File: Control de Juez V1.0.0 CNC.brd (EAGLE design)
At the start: 35.5 x 58.4 mm, 31 parts, among them IC1 MEGA48/88/168-AU, Q1 MMBT3904, Q2 MMBT3904, Q3 MMBT3904, SW1 JS202011CQN, SW2 3-1825910-1, SW3 3-1825910-1, SW4 3-1825910-1

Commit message: Add files via upload
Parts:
- removed C2, C3: 0.1uF, rcl:C0603
- removed IC1: MEGA48/88/168-AU, avr-8:TQFP32-08
- removed JP2: (no value), pinhead-2:1X04-S
- removed L1: 10uH, rcl:L1812
- removed R1, R7, R8, R9: 10K, rcl:R0603
- removed SW1: JS202011CQN, C&K-Slider_Switch:PTH
- added PROG: (no value), pinhead:1X03
- added S1: JS102011SAQN, JS102011SAQN:SW_JS102011SAQN
- added U1: ATTINY412-SSNSOIC8_SA_SST_MCH-M, attiny412:SOIC8_SA_SST_MCH-M
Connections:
- removed net N$2: C3.1, IC1.18, L1.1
- removed net N$3: C2.1, IC1.20
- removed net N$4: IC1.16, JP2.1
- removed net N$5: IC1.17, JP2.2
- removed net N$6: JP3.1, SW1.1.1, SW1.1.2, SW1.2.1, SW1.2.2
- removed net RESET: IC1.29, JP2.3, R1.1
- new net BAT+: JP3.1, S1.2, S1.3
- net +5V: now also PROG.1, S1.1, U1.1; no longer IC1.4, IC1.6, L1.2, R1.2, R7.2, R8.2, R9.2, SW1.3.1, SW1.3.2
- net GND: now also PROG.3, U1.8; no longer C2.2, C3.2, IC1.21, IC1.3, IC1.5
- net GO: now also U1.3; no longer IC1.31, R9.1
- net LEDS: now also U1.5; no longer IC1.13
- net LEDSMD: now also U1.4; no longer IC1.32
- net N$1: now also PROG.2, U1.6; no longer IC1.15, JP2.4
- net READY: now also U1.2; no longer IC1.1, R7.1
- net RST: now also U1.7; no longer IC1.30, R8.1
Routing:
- net +5V: track 203.4 -> 62.7 mm, vias 4 -> 1
- net GND: track 130.3 -> 58.4 mm, vias 5 -> 3
- net LEDS: track 91.3 -> 42.3 mm
- net GO: track 48.5 -> 6.50 mm, vias 1 -> 0
- net RESET: track 29.4 -> 0.00 mm, vias 2 -> 0
- net READY: track 34.2 -> 6.51 mm, vias 1 -> 0
- net RST: track 33.0 -> 6.51 mm, vias 2 -> 0
- net N$2: track 17.3 -> 0.00 mm
- net LEDSMD: track 46.1 -> 29.0 mm
- net N$6: track 13.3 -> 0.00 mm
- net N$1: track 13.1 -> 0.00 mm, vias 1 -> 0
- net N$5: track 10.4 -> 0.00 mm, vias 1 -> 0
- net N$3: track 10.1 -> 0.00 mm
- net N$4: track 8.63 -> 0.00 mm, vias 1 -> 0

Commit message: Add files via upload
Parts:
- removed JP1, JP3: (no value), pinhead-2:1X02-S
- removed LED4: (no value), led:CHIP-LED0603
- removed PROG: (no value), pinhead:1X03
- removed Q2, Q3: MMBT3904, FAIRCHILD-MMBT3904_Transistor:SOT23
- removed R3, R4: 1K, rcl:R0603
- removed R5: 330E, rcl:R0603
- removed SW2, SW3, SW4: 3-1825910-1, TE-Push_button:TE_3-1825910-1
- added BT2: BU2032SM-HD-G, BU2032SM-HD-G:BAT_BU2032SM-HD-G
- added GND, UPDI, V+: TPB1,27, testpad:B1,27
- added GO, READY, RESET: EVQ-P7L01P, EVQ-P7L01P:SW_EVQ-P7L01P
- added GOLD_ORB_SM1: OSHWLOGOLOGO8MM, oshw:OSHW_8MM
- added R1: 1K, rcl:R0603
- BT1: value HOLD-BATTERY-3-AAA -> BU2032SM-HD-G; device BATTERY_HOLDER_3AAA-C9091:HOLDER-3-AAA -> BU2032SM-HD-G:BAT_BU2032SM-HD-G
- LED5: device led:CHIP-LED0603 -> led:SML1206
- R6: value 330E -> 1k
- moved U1 55.7 mm to (17.9, 48.9), flipped to the bottom
- moved S1 53.9 mm to (2.54, 53.3), flipped to the bottom
- moved C4 49.9 mm to (17.8, 55.2), flipped to the bottom, turned to 0 degrees
- moved C1 46.6 mm to (17.8, 52.7), flipped to the bottom, turned to 0 degrees
- moved Q1 21.6 mm to (11.4, 61.0), flipped to the bottom, turned to 270 degrees
- moved R2 21.6 mm to (15.2, 61.0), flipped to the bottom, turned to 270 degrees
- moved LED5 16.3 mm to (25.9, 58.2), flipped to the bottom
- moved R6 15.3 mm to (19.9, 58.4), flipped to the bottom, turned to 180 degrees
- moved BT1 15.2 mm to (17.8, 11.5), flipped to the bottom
- moved LED1 8.89 mm to (31.8, 64.8)
- moved LED2 8.89 mm to (17.8, 64.8), flipped to the bottom
- moved LED3 8.89 mm to (3.81, 64.8)
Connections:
- removed net BAT+: JP3.1, S1.2, S1.3
- removed net N$10: Q3.B, R4.1
- removed net N$11: Q2.B, R3.1
- removed net N$13: LED5.C, R5.1
- removed net N$15: LED4.A, R5.2
- removed net N$7: LED1.2, Q1.C
- removed net N$8: LED2.2, Q2.C
- removed net N$9: LED3.2, Q3.C
- new net N$2: BT1.-, BT2.-, S1.1, S1.2
- new net N$3: LED1.2, LED2.2, LED3.2, R1.1
- new net N$4: Q1.C, R1.2
- net +5V: now also BT1.+, BT2.+, V+.TP; no longer JP1.1, PROG.1, S1.1
- net GND: now also GND.TP, GO.1_1, GO.1_2, READY.1_1, READY.1_2, RESET.1_1, RESET.1_2, S1.3; no longer JP1.2, JP3.2, PROG.3, Q2.E, Q3.E, SW2.1, SW2.2, SW3.1, SW3.2, SW4.1, SW4.2
- net GO: now also GO.2_1, GO.2_2; no longer SW4.3, SW4.4
- net LEDS: no longer R3.2, R4.2
- net LEDSMD: now also LED5.C; no longer LED4.C
- net N$1: now also UPDI.TP; no longer PROG.2
- net READY: now also READY.2_1, READY.2_2; no longer SW2.3, SW2.4
- net RST: now also RESET.2_1, RESET.2_2; no longer SW3.3, SW3.4
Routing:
- net +5V: track 62.7 -> 129.4 mm, vias 1 -> 2
- net N$2: track 0.00 -> 42.9 mm
- net N$3: track 0.00 -> 33.3 mm
- net READY: track 6.51 -> 25.6 mm, vias 0 -> 2
- net GND: track 58.4 -> 77.2 mm, vias 3 -> 4
- net N$13: track 18.4 -> 0.00 mm, vias 2 -> 0
- net LEDS: track 42.3 -> 24.3 mm
- net RST: track 6.51 -> 22.5 mm, vias 0 -> 2
- net N$8: track 12.8 -> 0.00 mm, vias 1 -> 0
- net LEDSMD: track 29.0 -> 17.0 mm
- net GO: track 6.50 -> 17.9 mm, vias 0 -> 2
- net N$9: track 7.59 -> 0.00 mm, vias 1 -> 0
- net N$7: track 4.80 -> 0.00 mm, vias 1 -> 0
- net N$10: track 4.03 -> 0.00 mm
- net N$11: track 4.03 -> 0.00 mm
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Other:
- board size 35.5 x 58.4 mm -> 35.5 x 67.3 mm
- board text added: "Apagado"
- board text added: "Control Juez Anti Fuckin' Monopolio CNC V1.1.0"
- board text added: "Diseñado en México por Sol y Nomada-e"
- board text added: "Encendido"
- board text added: "GO"
- board text added: "READY"
- board text added: "RESET"
- board text removed: "Control Juez Anti Fuckin' Monopolio CNC V1.0.0"

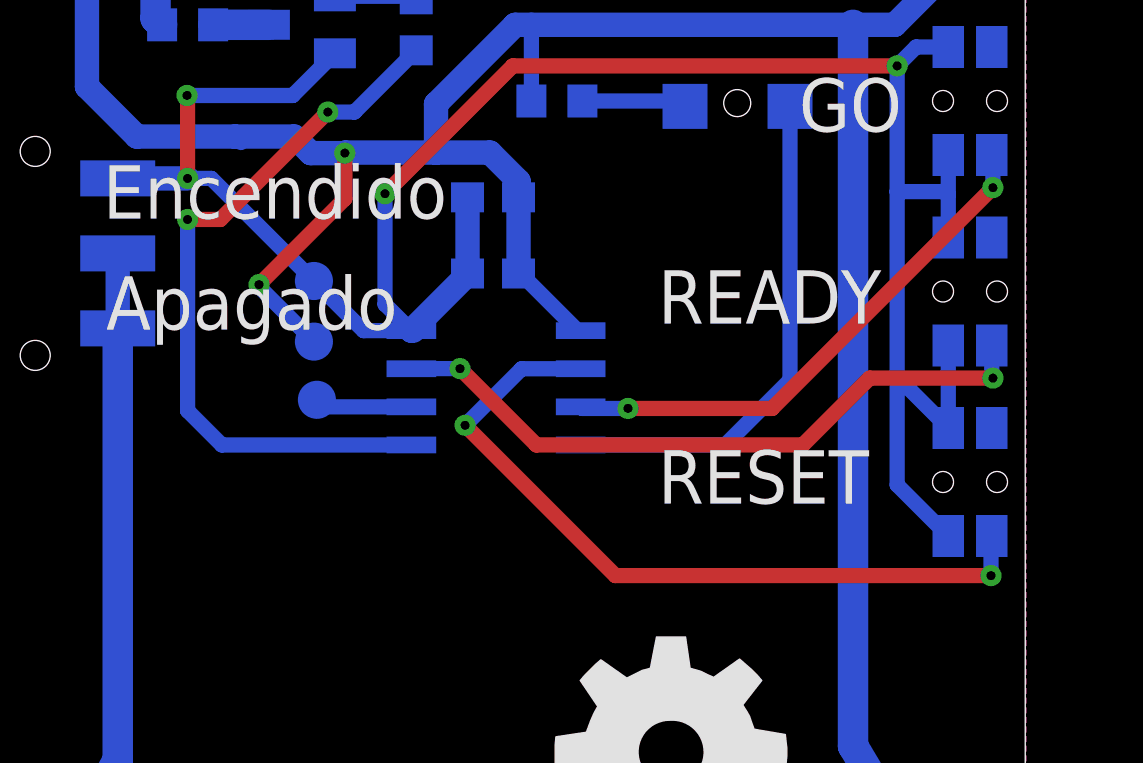
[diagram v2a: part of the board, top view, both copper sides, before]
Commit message: Add files via upload
Reconexiones para mejor programación ocupando el hardware del microcontrolador
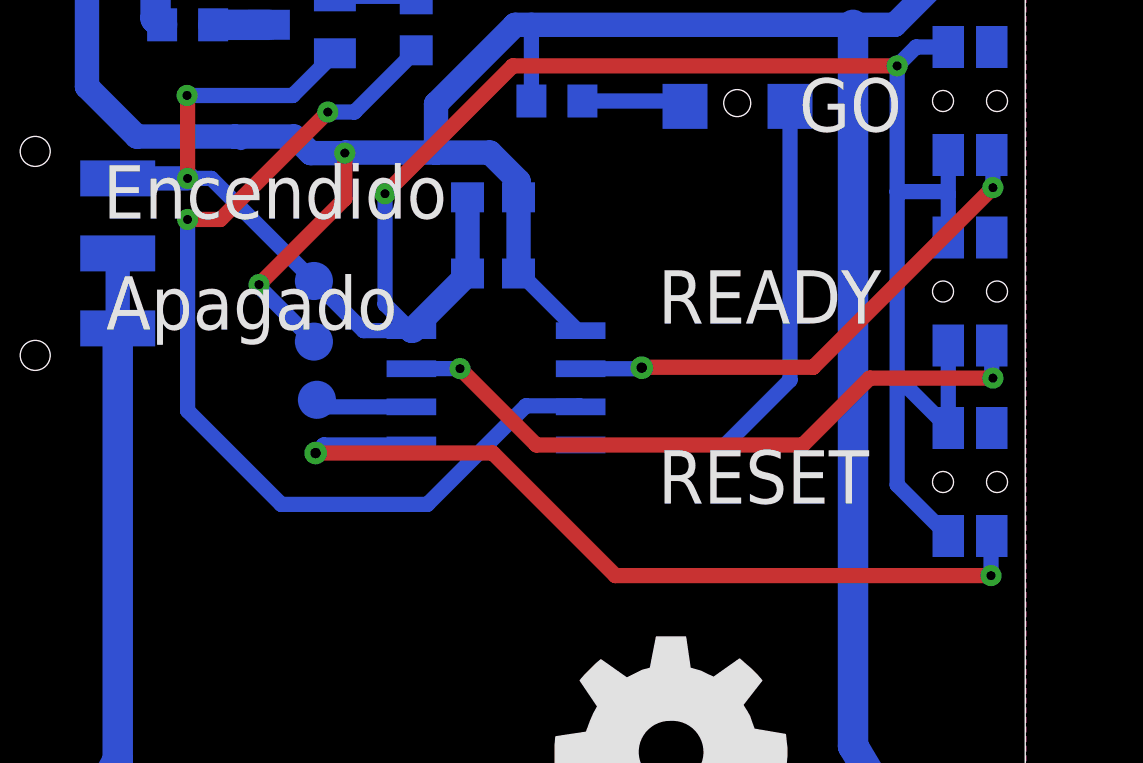
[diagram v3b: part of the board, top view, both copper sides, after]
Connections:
- net GO: now also U1.2; no longer U1.3
- net LEDS: now also U1.3; no longer U1.5
- net READY: now also U1.5; no longer U1.2
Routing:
- net LEDS: track 24.3 -> 32.1 mm
- net LEDSMD: track 17.0 -> 12.2 mm
- net READY: track 25.6 -> 28.8 mm
- net GO: track 17.9 -> 17.3 mm
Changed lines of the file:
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@@
 <signal name="LEDS">
 <contactref element="R2" pad="2"/>
-<contactref element="U1" pad="5"/>
 <wire x1="15.24" y1="60.11" x2="13.181775" y2="58.051775" width="0.508" layer="16"/>
 <wire x1="13.181775" y1="58.051775" x2="12.29259375" y2="58.051775" width="0.508" layer="16"/>
@@
 <wire x1="8.71161875" y1="54.4708" x2="7.62" y2="54.4708" width="0.508" layer="1"/>
 <via x="7.62" y="54.4708" extent="1-16" drill="0.3"/>
-<wire x1="7.62" y1="48.0947" x2="8.7597" y2="46.955" width="0.508" layer="16"/>
-<wire x1="8.7597" y1="46.955" x2="15.07865" y2="46.955" width="0.508" layer="16"/>
 <wire x1="7.62" y1="54.4708" x2="7.62" y2="48.0947" width="0.508" layer="16"/>
+<contactref element="U1" pad="3"/>
+<wire x1="10.7405" y1="44.9742" x2="15.6118" y2="44.9742" width="0.508" layer="16"/>
+<wire x1="15.6118" y1="44.9742" x2="18.8976" y2="48.26" width="0.508" layer="16"/>
+<wire x1="18.8976" y1="48.26" x2="20.68635" y2="48.26" width="0.508" layer="16"/>
+<wire x1="20.68635" y1="48.26" x2="20.72135" y2="48.225" width="0.508" layer="16"/>
+<wire x1="7.62" y1="48.0947" x2="10.7405" y2="44.9742" width="0.508" layer="16"/>
 </signal>
 <signal name="N$14">
@@
 </signal>
 <signal name="LEDSMD">
-<contactref element="U1" pad="4"/>
 <contactref element="LED5" pad="C"/>
-<wire x1="20.72135" y1="46.955" x2="25.54" y2="46.955" width="0.508" layer="16"/>
 <wire x1="25.54" y1="46.955" x2="27.7" y2="49.115" width="0.508" layer="16"/>
 <wire x1="27.7" y1="49.115" x2="27.7" y2="58.24" width="0.508" layer="16"/>
+<contactref element="U1" pad="4"/>
+<wire x1="20.72135" y1="46.955" x2="25.54" y2="46.955" width="0" layer="19" extent="16-16"/>
 </signal>
 <signal name="RST">
@@
 <wire x1="30.3545125" y1="49.1828" x2="28.1267125" y2="46.955" width="0.508" layer="1"/>
 <wire x1="28.1267125" y1="46.955" x2="19.245" y2="46.955" width="0.508" layer="1"/>
-<wire x1="19.245" y1="46.955" x2="16.7" y2="49.5" width="0.508" layer="1"/>
 <wire x1="16.7" y1="49.5" x2="15.08365" y2="49.5" width="0.508" layer="16"/>
 <wire x1="15.08365" y1="49.5" x2="15.07865" y2="49.495" width="0.508" layer="16"/>
+<wire x1="19.245" y1="46.955" x2="16.7" y2="49.5" width="0.508" layer="1"/>
 <wire x1="34.425" y1="50.27" x2="34.425" y2="53.87" width="0" layer="19" extent="16-16"/>
 </signal>
 <signal name="GO">
-<contactref element="U1" pad="3"/>
 <contactref element="GO" pad="2_2"/>
 <contactref element="GO" pad="2_1"/>
@@
 <wire x1="34.4628" y1="56.5822" x2="34.4628" y2="55.5328" width="0.508" layer="16"/>
 <via x="34.4628" y="55.5328" extent="1-16" drill="0.3"/>
-<wire x1="34.4628" y1="55.5328" x2="27.1018" y2="48.1718" width="0.508" layer="1"/>
-<wire x1="27.1018" y1="48.1718" x2="22.3" y2="48.1718" width="0.508" layer="1"/>
-<via x="22.3" y="48.1718" extent="1-16" drill="0.3"/>
-<wire x1="22.3" y1="48.1718" x2="20.77455" y2="48.1718" width="0.508" layer="16"/>
-<wire x1="20.77455" y1="48.1718" x2="20.72135" y2="48.225" width="0.508" layer="16"/>
+<wire x1="34.4628" y1="55.5328" x2="28.4734" y2="49.5434" width="0.508" layer="1"/>
+<contactref element="U1" pad="2"/>
+<wire x1="28.4734" y1="49.5434" x2="22.7718" y2="49.5434" width="0.508" layer="1"/>
+<wire x1="22.7584" y1="49.53" x2="22.7718" y2="49.5434" width="0.508" layer="1"/>
+<via x="22.7584" y="49.53" extent="1-16" drill="0.35"/>
+<wire x1="22.7584" y1="49.53" x2="22.7234" y2="49.495" width="0.508" layer="16"/>
+<wire x1="22.7234" y1="49.495" x2="20.72135" y2="49.495" width="0.508" layer="16"/>
 <wire x1="34.425" y1="56.62" x2="34.425" y2="60.22" width="0" layer="19" extent="16-16"/>
 </signal>
 <signal name="READY">
-<contactref element="U1" pad="2"/>
 <contactref element="READY" pad="2_2"/>
 <contactref element="READY" pad="2_1"/>
@@
 <via x="34.4" y="42.6" extent="1-16" drill="0.3"/>
 <wire x1="34.4" y1="42.6" x2="21.87918125" y2="42.6" width="0.508" layer="1"/>
-<wire x1="21.87918125" y1="42.6" x2="16.8689" y2="47.61028125" width="0.508" layer="1"/>
-<via x="16.8689" y="47.61028125" extent="1-16" drill="0.3"/>
-<wire x1="16.8689" y1="47.61028125" x2="18.75361875" y2="49.495" width="0.508" layer="16"/>
-<wire x1="18.75361875" y1="49.495" x2="20.72135" y2="49.495" width="0.508" layer="16"/>
+<contactref element="U1" pad="5"/>
+<wire x1="21.87918125" y1="42.6" x2="17.79398125" y2="46.6852" width="0.508" layer="1"/>
+<wire x1="17.79398125" y1="46.6852" x2="11.8872" y2="46.6852" width="0.508" layer="1"/>
+<via x="11.8872" y="46.6852" extent="1-16" drill="0.35"/>
+<wire x1="11.8872" y1="46.6852" x2="12.157" y2="46.955" width="0.508" layer="16"/>
+<wire x1="12.157" y1="46.955" x2="15.07865" y2="46.955" width="0.508" layer="16"/>
 <wire x1="34.425" y1="43.92" x2="34.425" y2="47.52" width="0" layer="19" extent="16-16"/>
 </signal>

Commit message: Add files via upload
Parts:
- moved Q1 4.93 mm to (11.4, 65.9)
- moved R1 4.93 mm to (7.62, 65.9)
- moved R2 4.93 mm to (15.2, 65.9)
- moved C1 4.93 mm to (17.8, 57.6)
- moved C4 4.93 mm to (17.8, 60.1)
- moved GND 4.93 mm to (11.8, 57.3)
- moved GO 4.93 mm to (33.7, 63.3)
- moved LED1 4.93 mm to (31.8, 69.7)
- moved LED2 4.93 mm to (17.8, 69.7)
- moved LED3 4.93 mm to (3.81, 69.7)
- moved LED5 4.93 mm to (25.9, 63.2)
- moved R6 4.93 mm to (19.9, 63.3)
- moved READY 4.93 mm to (33.7, 50.6)
- moved RESET 4.93 mm to (33.7, 57.0)
- moved S1 4.93 mm to (2.54, 58.3)
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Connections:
- net LEDSMD renamed LEDSTATUS
- removed net LEDS: R2.2, U1.3
- removed net RST: RESET.2_1, RESET.2_2, U1.7
- new net LEDTRANSMISION: R2.2, U1.5
- new net RESET: READY.2_1, READY.2_2, U1.2
- net GO: now also U1.3; no longer U1.2
- net READY: now also RESET.2_1, RESET.2_2, U1.7; no longer READY.2_1, READY.2_2, U1.5
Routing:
- net LEDS: track 32.1 -> 0.00 mm, vias 2 -> 0
- net RESET: track 0.00 -> 25.6 mm, vias 0 -> 2
- net LEDTRANSMISION: track 0.00 -> 24.3 mm, vias 0 -> 2
- net RST: track 22.5 -> 0.00 mm, vias 2 -> 0
- net +5V: track 129.4 -> 136.3 mm
- net READY: track 28.8 -> 22.5 mm
- net N$2: track 42.9 -> 47.9 mm
- net LEDSTATUS: track 12.2 -> 17.0 mm
- net GO: track 17.3 -> 17.9 mm
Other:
- board size 35.5 x 67.3 mm -> 35.5 x 72.2 mm

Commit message: Add files via upload
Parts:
- removed U1: ATTINY412-SSNSOIC8_SA_SST_MCH-M, attiny412:SOIC8_SA_SST_MCH-M
- added U2: ATTINY1614-SSNR, Attiny1614:SOIC14_SL_MCH
- moved GOLD_ORB_SM1 16.3 mm to (8.37, 42.3)
- moved C1 0.61 mm to (17.8, 58.2)
- moved C4 0.26 mm to (17.9, 60.4)
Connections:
- removed net N$1: U1.6, UPDI.TP
- new net UPDI: U2.10, UPDI.TP
- net +5V: now also U2.1; no longer U1.1
- net GND: now also U2.14; no longer U1.8
- net GO: now also U2.5; no longer U1.3
- net LEDSTATUS: now also U2.6; no longer U1.4
- net LEDTRANSMISION: now also U2.2; no longer U1.5
- net READY: now also U2.4; no longer U1.7
- net RESET: now also U2.7; no longer U1.2
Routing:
- net LEDTRANSMISION: track 24.3 -> 36.8 mm
- net RESET: track 25.6 -> 15.9 mm
- net READY: track 22.5 -> 17.9 mm
- net UPDI: track 0.00 -> 3.84 mm
- net N$1: track 3.25 -> 0.00 mm
- net LEDSTATUS: track 17.0 -> 19.3 mm
- net GO: track 17.9 -> 19.5 mm
- net +5V: track 136.3 -> 135.7 mm
